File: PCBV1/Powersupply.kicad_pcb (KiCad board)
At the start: 4 copper layers, 145 x 99.1 mm, 132 parts, among them J1 Conn_01x02, J2 Conn_WallPlug, J3 QSH-030-01-F-D-A-K-TR, J4 20021121-00010C4LF, J5 Conn_01x02, J6 Conn_01x02, J7 Conn_01x02, J8 Conn_01x07, T1 EFD 20/10/7, U1 ST1S41PHR, U2 ST1S41PHR, U3 VIPER318HDTR, U4 STM32F469IITx, U5 IS42S16400J-xT, U6 W25Q32JVSS, X1 ECS-5032MV-100-BN-TR

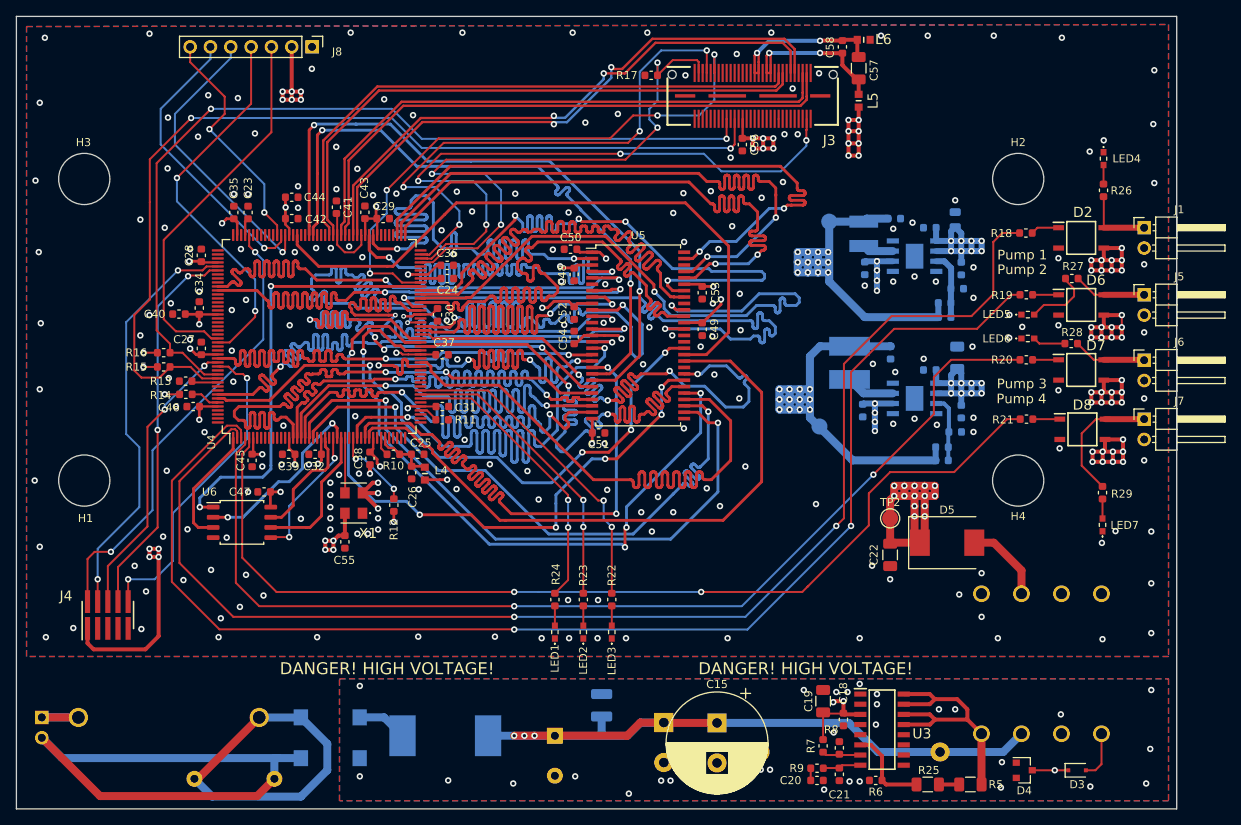
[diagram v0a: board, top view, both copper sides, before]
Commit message: Changed ferrite beads to ones with adequate max currents. Changed JTAG connector to 20-pin standard. Minor PCB fixes.
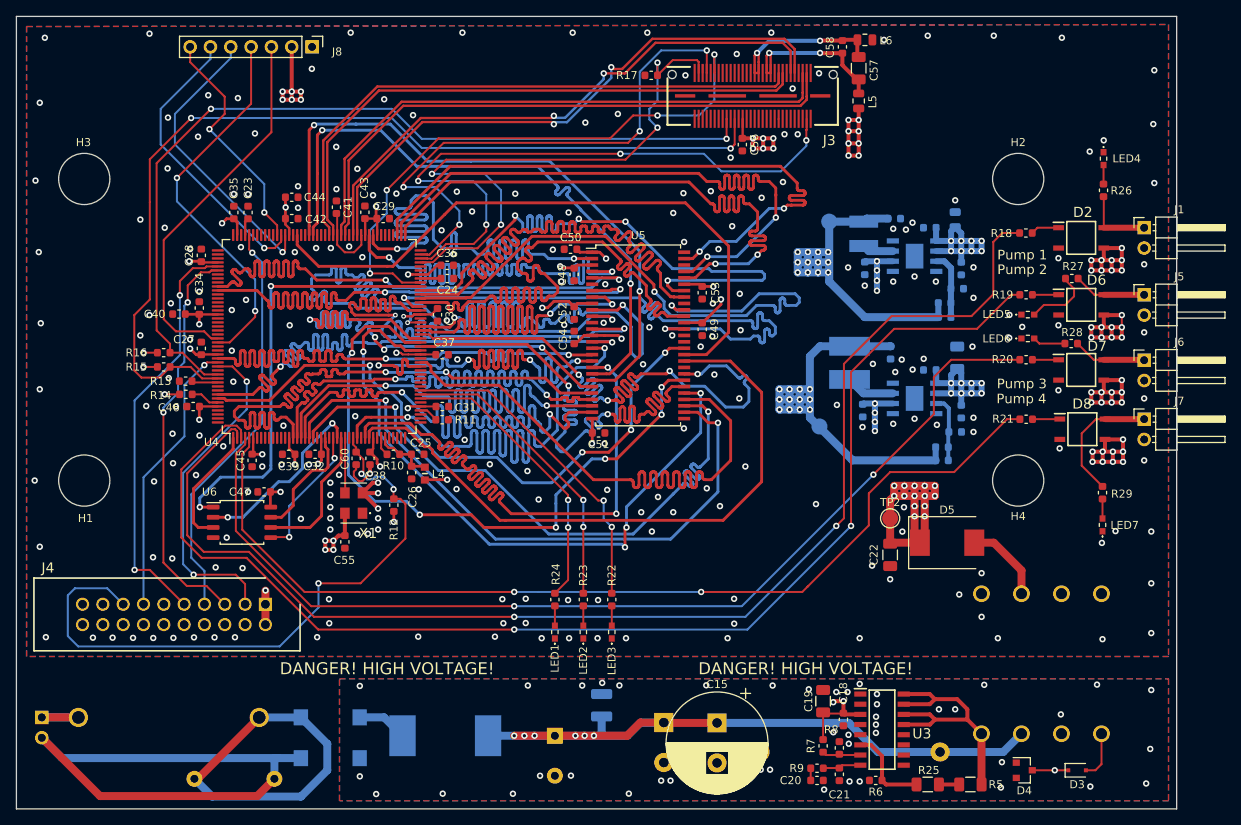
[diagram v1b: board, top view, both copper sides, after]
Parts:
- added C60: 100 nF, Capacitor_SMD:C_0603_1608Metric, F.Cu at (126.3, 73.0)
- J4: value 20021121-00010C4LF -> 61202021621; footprint SamacSys_Parts:HUSSP10W40P127_2X5_635X340X420P -> SamacSys_Parts:SHDR20W64P254_2X10_3306X910X885P
- L5, L6: value BK1608HS601-T -> 120 R @ 100 MHz, 6 A; footprint SamacSys_Parts:BEADC1608X95N -> Inductor_SMD:L_0805_2012Metric
- moved J4 19.7 mm to (114.9, 91.3), turned to 180 degrees
- moved L6 0.15 mm to (189.9, 20.7), turned to 180 degrees
- turned L5 to 270 degrees
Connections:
- J4 pad 10: /MCU/NJTRST -> GND
- J4 pad 2: /MCU/JTMS_SWDIO -> 3V3
- J4 pad 3: GND -> /MCU/JNTRST
- J4 pad 4: /MCU/JTCK_SWCLK -> GND
- J4 pad 5: GND -> /MCU/JTDI
- J4 pad 6: /MCU/JTDO_TRACESWO -> GND
- J4 pad 7: Net-(J4-Pad7) -> /MCU/JTMS_SWDIO
- J4 pad 8: /MCU/JTDI -> GND
- J4 pad 9: GND -> /MCU/JTCK_SWCLK
- L5 pad 1: 5V -> Net-(C57-Pad1)
- L5 pad 2: Net-(C57-Pad1) -> 5V
- L6 pad 1: Net-(C57-Pad2) -> GND
- L6 pad 2: GND -> Net-(C57-Pad2)
- R12 pad 2: Net-(R12-Pad2) -> /MCU/NRST
- U4 pad 162: /MCU/NJTRST -> /MCU/JNTRST
- U4 pad 31: Net-(R12-Pad2) -> /MCU/NRST
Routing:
- net /MCU/NRST: track 0.00 -> 80.9 mm, vias 0 -> 3
- net /MCU/JNTRST: track 0.00 -> 41.9 mm, vias 0 -> 2
- net /MCU/NJTRST: track 40.3 -> 0.00 mm, vias 2 -> 0
- net 3V3: track 233.9 -> 212.2 mm, vias 60 -> 57
- net Net-(R12-Pad2): track 10.3 -> 0.00 mm, vias 2 -> 0
- net /MCU/JTMS_SWDIO: track 56.8 -> 51.2 mm, vias 2 -> 1
- net MCPump2On: track 162.4 -> 157.7 mm
- net GND: track 8.36 -> 12.6 mm, vias 210 -> 229
- net MCPump3On: track 133.3 -> 129.5 mm
- net MCPump1On: track 163.9 -> 160.5 mm
- net MCPump4On: track 125.8 -> 123.7 mm
- net /MCU/JTDI: track 48.3 -> 50.3 mm
- net /MCU/JTDO_TRACESWO: track 36.3 -> 34.9 mm, vias 2 -> 1
- net Net-(C14-Pad1): vias 3 -> 6
- net GNDREF: vias 32 -> 46

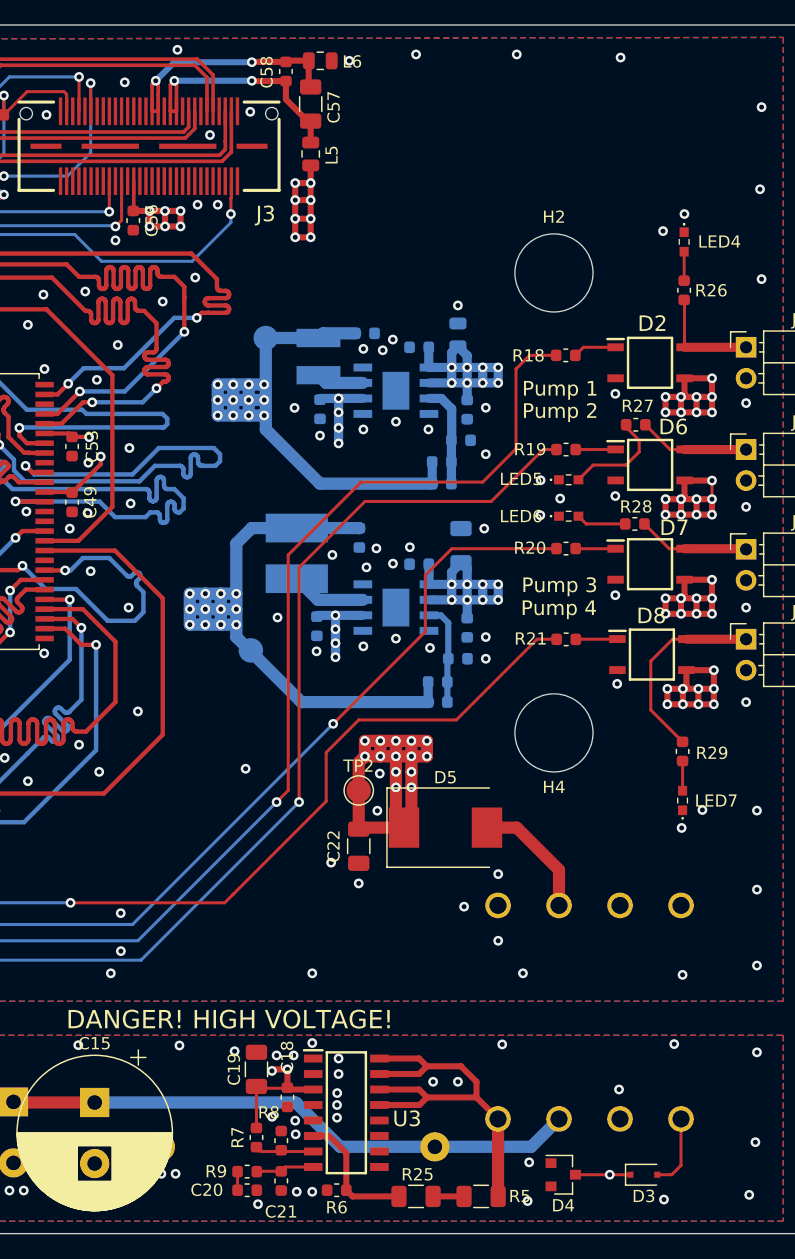
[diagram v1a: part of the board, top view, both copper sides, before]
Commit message: Made changes to PCB (added many planes/polygons instead of traces, increased amount of vias, increased trace sizes).
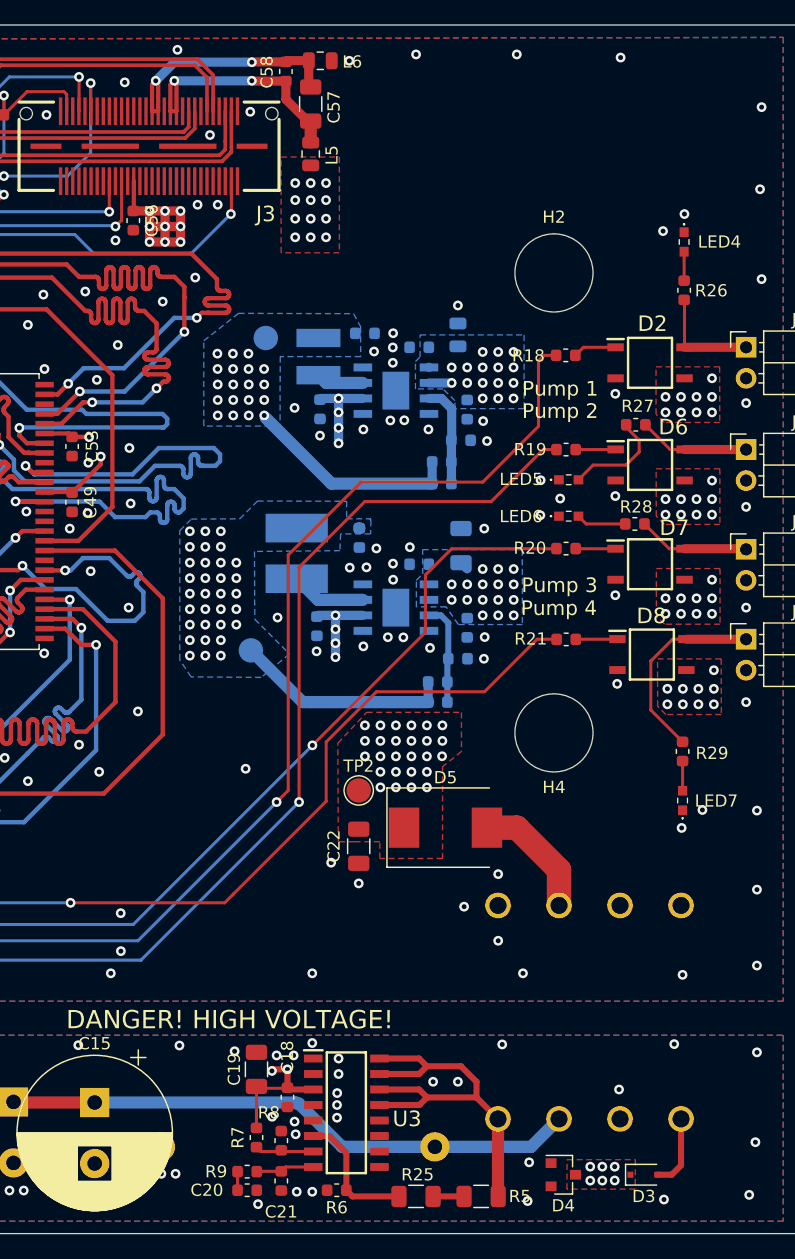
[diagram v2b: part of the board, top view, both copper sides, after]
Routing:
- net 12V: track 172.7 -> 19.1 mm, vias 74 -> 102
- net 5V: track 69.3 -> 17.8 mm, vias 20 -> 31
- net 3V3: track 212.2 -> 177.1 mm, vias 57 -> 80
- net Net-(C18-Pad1): track 15.5 -> 11.0 mm, vias 3 -> 8
- net LCD_INT: track 79.4 -> 78.4 mm
- net MCPump1On: track 160.5 -> 159.8 mm
- net MCPump4On: track 123.7 -> 124.2 mm
- net GND: vias 229 -> 231
- added copper zone on B.Cu, net 12V
- added copper zone on F.Cu, net 12V
- added copper zone on B.Cu, net 3V3
- added copper zone on B.Cu, net 5V
- added copper zone on F.Cu, net 5V
- added copper zone on F.Cu, net Net-(C18-Pad1)

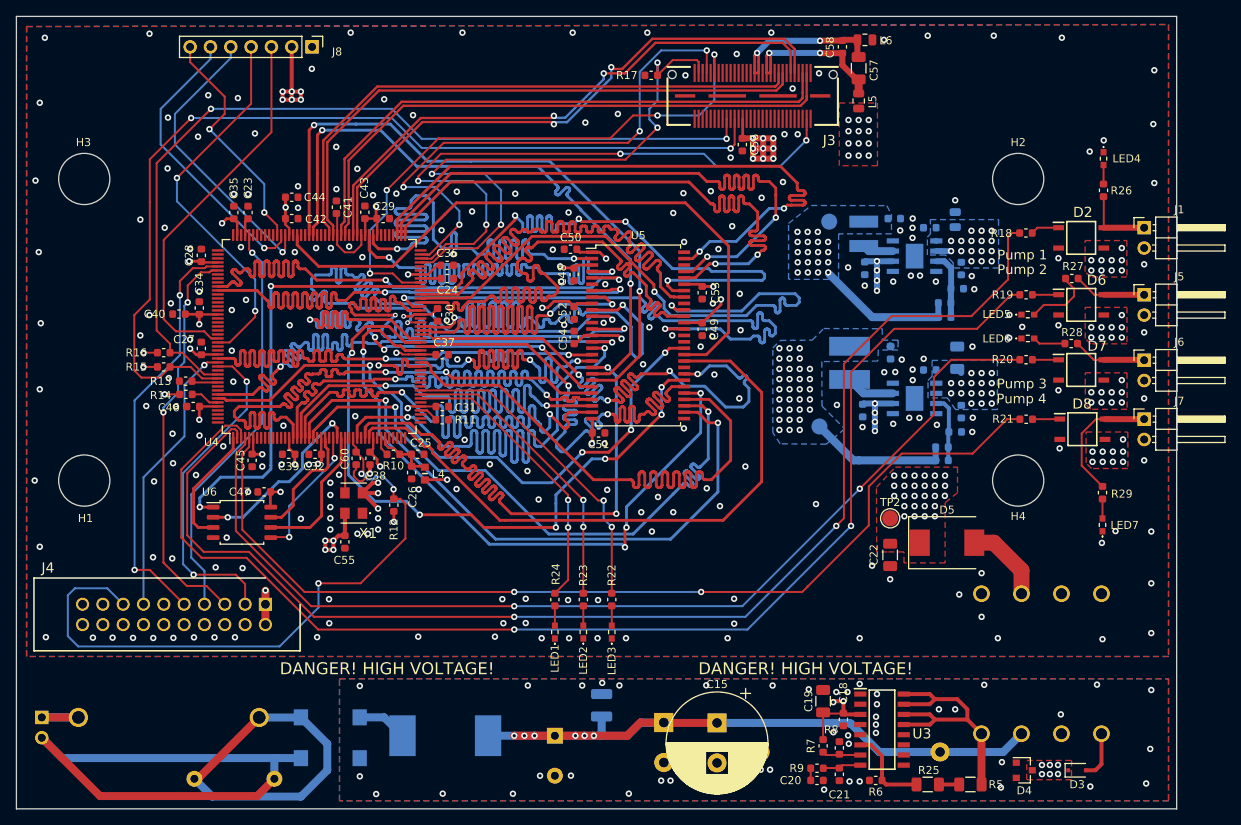
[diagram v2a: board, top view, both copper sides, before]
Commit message: Added new JTAG/UART header with connections for STLink V3. Moved from SamacSys to personal GitHub-based library.
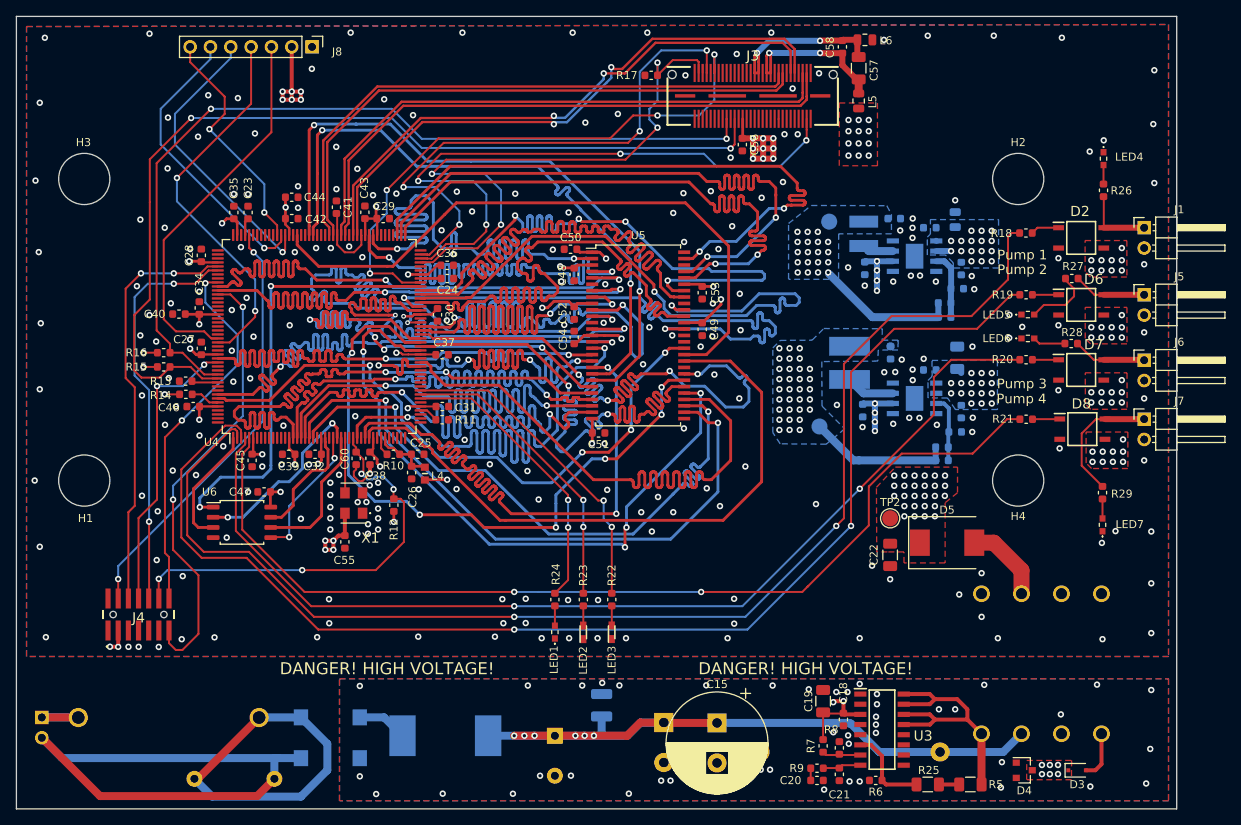
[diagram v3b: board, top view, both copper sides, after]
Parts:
- D1: footprint SamacSys_Parts:YBS2207GRAG -> Personal_Passives:YBS2207G_RAG
- D2, D6, D7, D8: footprint SamacSys_Parts:SOP254P610X218-4N -> Personal_ICs:CPC1020N
- F1: footprint SamacSys_Parts:646-SERIESHOLDER -> Personal_Misc:64600001003
- J3: footprint SamacSys_Parts:QSH-030-01-F-D-A -> Personal_Misc:QSH-030-01-F-D-A
- J4: value 61202021621 -> M50-3610742; footprint SamacSys_Parts:SHDR20W64P254_2X10_3306X910X885P -> SamacSys_Parts:M503610742R
- L1: footprint SamacSys_Parts:SRN6045TA220M -> Personal_Passives:SRN6045TA-101M
- L3: value 820 µH -> SRR1208-821KL; footprint SamacSys_Parts:INDPM127127X850N -> Personal_Passives:SRR1208-821KL
- L4: footprint SamacSys_Parts:BEADC1608X95N -> Personal_Passives:BK1608HS601-T
- LED1, LED4, LED5, LED6, LED7: footprint SamacSys_Parts:150060SS55040 -> Personal_Passives:150060SS55040
- LED2, LED3: footprint SamacSys_Parts:150060SS55040 -> Personal_Passives:150060VS55040
- U1, U2: footprint Package_SO:SOIC127P600X170-9N -> Personal_ICs:ST1S41PHR
- U3: footprint SamacSys_Parts:SOIC127P600X175-16N -> Personal_ICs:VIPER318HDTR
- X1: value ECS-5032MV-100-BN-TR -> ECS-5032MV-100-CN-TR; footprint SamacSys_Parts:ECS5032MV250CNTR -> Personal_Actives:ECS5032MV250CNTR
- moved J4 15.9 mm to (99.1, 92.5), turned to 0 degrees
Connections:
- J4 pad 1: 3V3 -> Net-(J4-Pad1)
- J4 pad 10: GND -> /MCU/JTDI
- J4 pad 11: Net-(J4-Pad11) -> GND
- J4 pad 12: GND -> /MCU/NRST
- J4 pad 13: /MCU/JTDO_TRACESWO -> UART5_RX
- J4 pad 14: GND -> UART5_TX
- J4 pad 2: 3V3 -> Net-(J4-Pad2)
- J4 pad 3: /MCU/JNTRST -> 3V3
- J4 pad 4: GND -> /MCU/JTMS_SWDIO
- J4 pad 5: /MCU/JTDI -> GND
- J4 pad 6: GND -> /MCU/JTCK_SWCLK
- J4 pad 7: /MCU/JTMS_SWDIO -> GND
- J4 pad 8: GND -> /MCU/JTDO_TRACESWO
- J4 pad 9: /MCU/JTCK_SWCLK -> Net-(J4-Pad9)
- U4 pad 141: Net-(U4-Pad141) -> UART5_TX
- U4 pad 144: Net-(U4-Pad144) -> UART5_RX
- U4 pad 162: /MCU/JNTRST -> Net-(U4-Pad162)
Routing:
- net UART5_RX: track 0.00 -> 56.0 mm, vias 0 -> 2
- net UART5_TX: track 0.00 -> 46.6 mm, vias 0 -> 2
- net /MCU/JNTRST: track 41.9 -> 0.00 mm, vias 2 -> 0
- net /MCU/NRST: track 80.9 -> 53.0 mm, vias 3 -> 4
- net GND: track 12.6 -> 5.45 mm, vias 231 -> 235
- net /MCU/JTMS_SWDIO: track 51.2 -> 53.6 mm, vias 1 -> 2
- net /MCU/JTDO_TRACESWO: track 34.9 -> 36.3 mm, vias 1 -> 2
- net 3V3: track 177.1 -> 175.9 mm, vias 80 -> 81

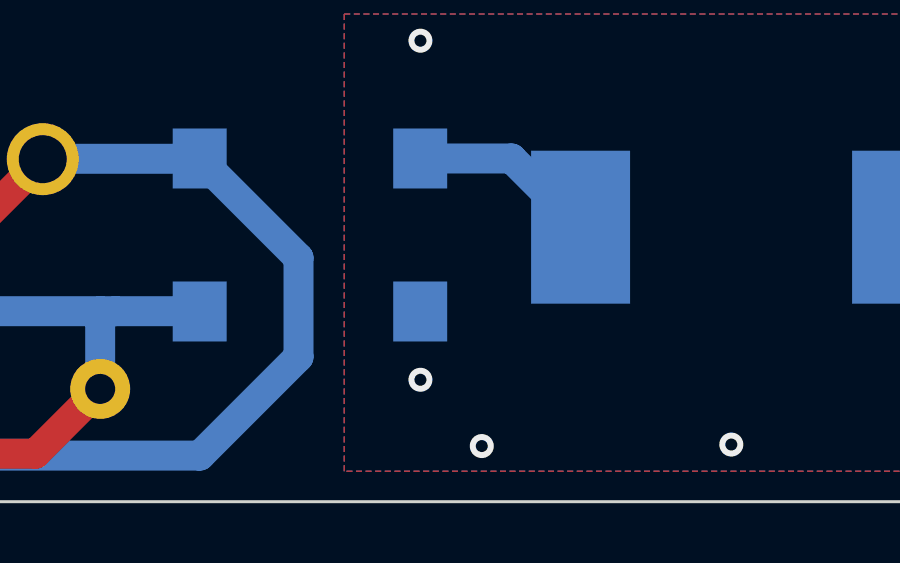
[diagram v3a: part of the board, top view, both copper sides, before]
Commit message: Updated schematic descriptions. Added converter test PCB.
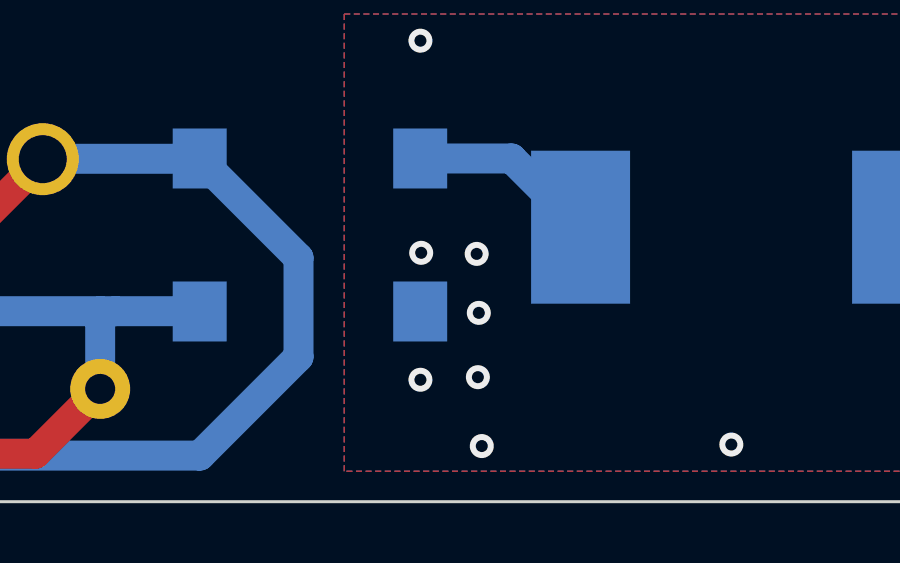
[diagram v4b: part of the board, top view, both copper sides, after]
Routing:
- net GNDREF: vias 46 -> 50
